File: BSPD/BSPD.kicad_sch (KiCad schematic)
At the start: 31 parts, among them Q101 Q_PMOS_GSD, U101 641964-1, U102 641964-1, U103 R-78E5.0-0.5, U104 SN74LVC1G08DBVR, U105 LM339DR, U106 NE555DR, U107 SN74LVC3G14DCUR, U108 SN74AC32DR, U109 SN74LVC1G08DBVR, U110 641964-1

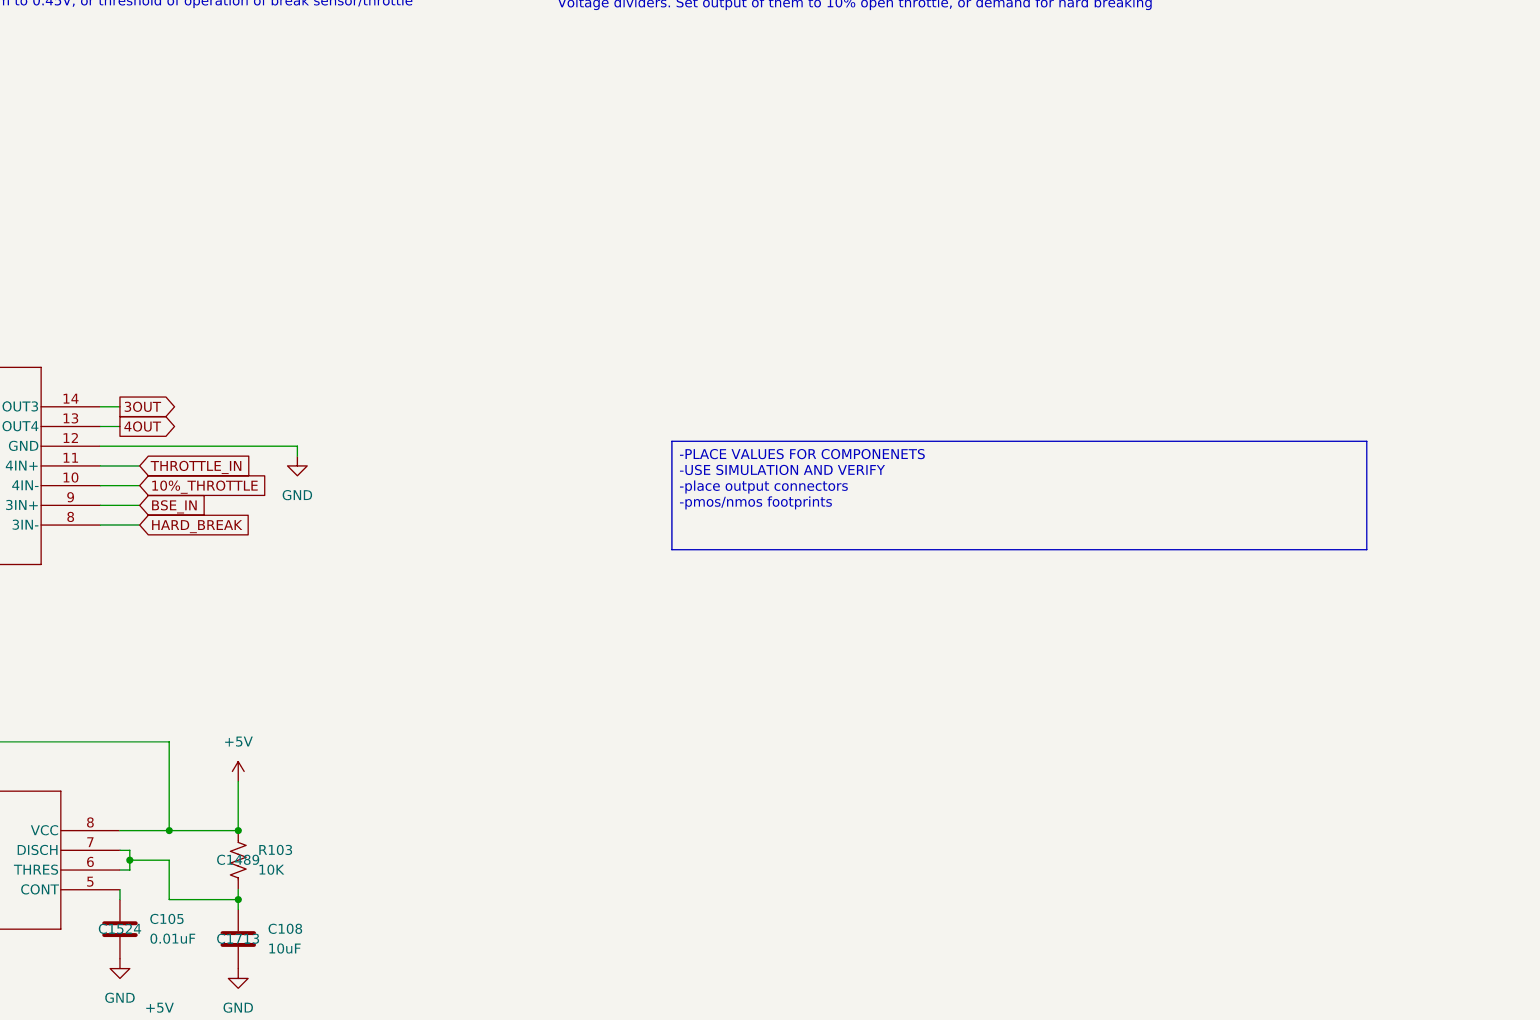
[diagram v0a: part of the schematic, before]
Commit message: Double checked PMOS output logic. Added connector and routing for sense wires from sensors. Connected one unconnected track. 2 DRC errors about spokes, but otherwise Ready to Geaux :3
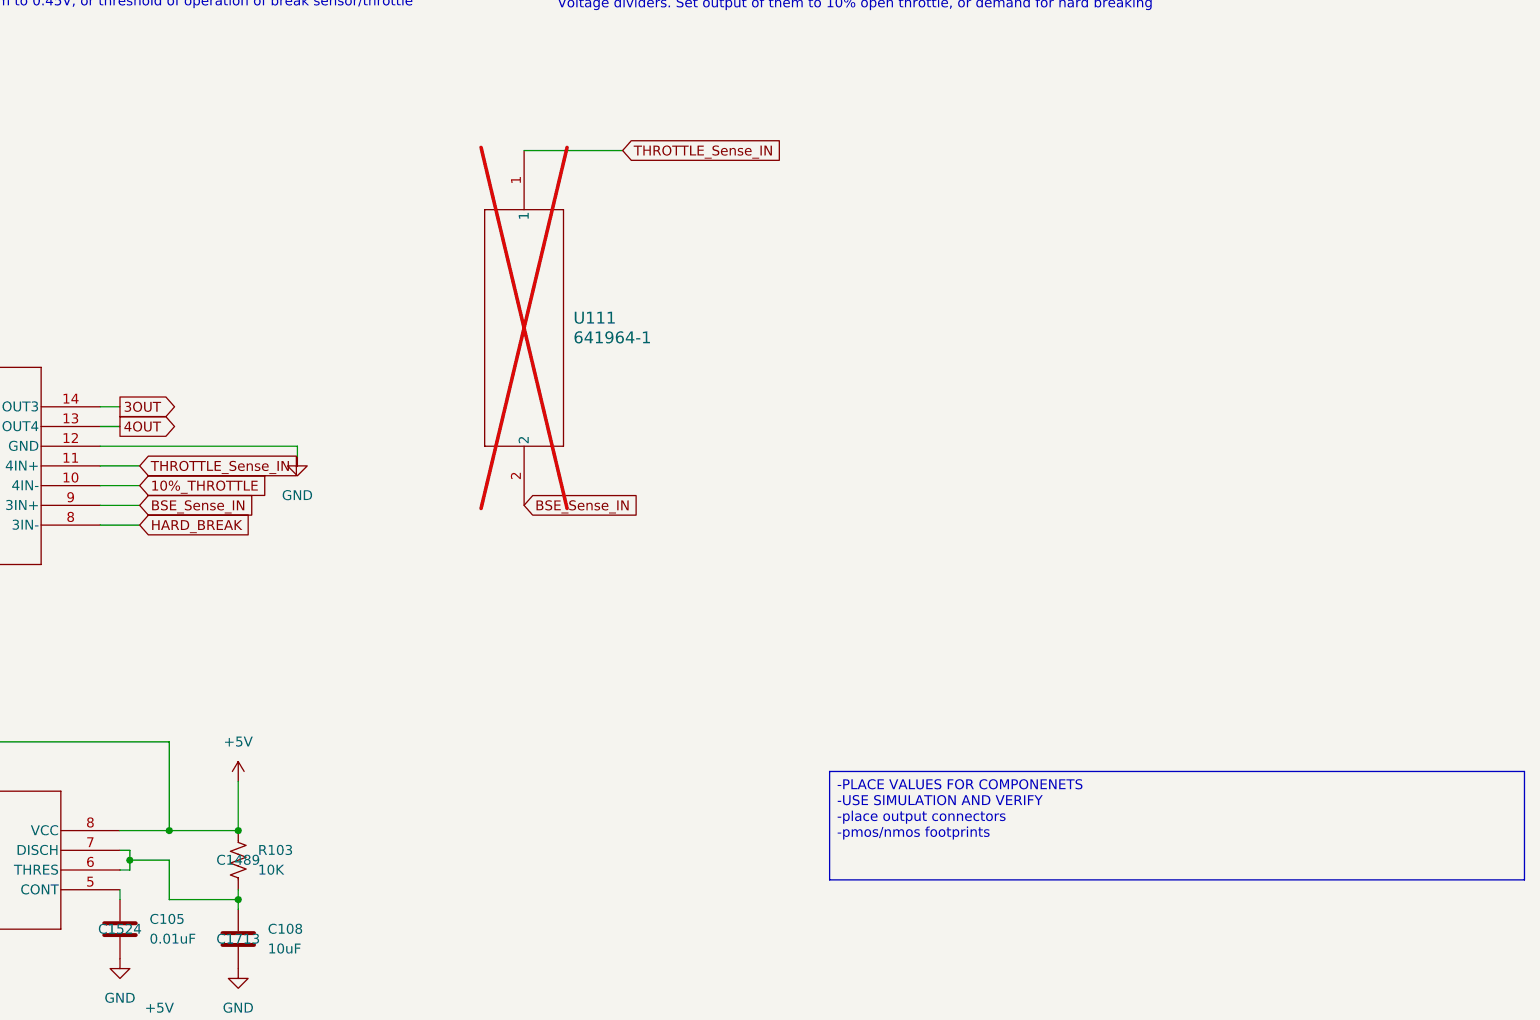
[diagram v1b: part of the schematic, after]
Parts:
- added U111: 641964-1, 641964-1:641964-1_TYC, symbol 641964-1:641964-1
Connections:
- net BSE_IN: no longer U105.9 (3IN+)
- net THROTTLE_IN: no longer U105.11 (4IN+)
- new net BSE_Sense_IN: U105.9 (3IN+), U111.2
- new net THROTTLE_Sense_IN: U105.11 (4IN+), U111.1
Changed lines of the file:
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@@
 	(text_box "-PLACE VALUES FOR COMPONENETS\n-USE SIMULATION AND VERIFY\n-place output connectors\n-pmos/nmos footprints\n\n"
 		(exclude_from_sim no)
-		(at 300.99 109.855 0)
+		(at 321.31 152.4 0)
 		(size 89.535 13.97)
 		(margins 0.9525 0.9525 0.9525 0.9525)
@@
 	(wire
 		(pts
+			(xy 294.64 72.39) (xy 281.94 72.39)
+		)
+		(stroke
+			(width 0)
+			(type default)
+		)
+	)
+	(wire
+		(pts
 			(xy 229.87 167.64) (xy 229.87 168.91)
 		)
@@
 		)
 	)
+	(global_label "BSE_Sense_IN"
+		(shape input)
+		(at 281.94 118.11 0)
+		(fields_autoplaced yes)
+		(effects
+			(font
+				(size 1.27 1.27)
+			)
+			(justify left)
+		)
+		(property "Intersheetrefs" "${INTERSHEET_REFS}"
+			(at 297.988 118.11 0)
+			(effects
+				(font
+					(size 1.27 1.27)
+				)
+				(justify left)
+				(hide yes)
+			)
+		)
+	)
 	(global_label "THRESH_BSE"
 		(shape input)
@@
 		)
 	)
-	(global_label "THROTTLE_IN"
+	(global_label "THROTTLE_Sense_IN"
 		(shape input)
 		(at 232.41 113.03 0)
@@
 		)
 		(property "Intersheetrefs" "${INTERSHEET_REFS}"
-			(at 247.309 113.03 0)
+			(at 253.8404 113.03 0)
 			(effects
 				(font
@@
 		)
 	)
-	(global_label "BSE_IN"
+	(global_label "BSE_Sense_IN"
 		(shape input)
 		(at 232.41 118.11 0)
@@
 		)
 		(property "Intersheetrefs" "${INTERSHEET_REFS}"
-			(at 241.9266 118.11 0)
+			(at 248.458 118.11 0)
 			(effects
 				(font
@@
 		)
 	)
+	(global_label "THROTTLE_Sense_IN"
+		(shape input)
+		(at 294.64 72.39 0)
+		(fields_autoplaced yes)
+		(effects
+			(font
+				(size 1.27 1.27)
+			)
+			(justify left)
+		)
+		(property "Intersheetrefs" "${INTERSHEET_REFS}"
+			(at 316.0704 72.39 0)
+			(effects
+				(font
+					(size 1.27 1.27)
+				)
+				(justify left)
+				(hide yes)
+			)
+		)
+	)
 	(global_label "THRESH_THROTTLE"
 		(shape input)
@@
 					(unit 1)
 				)
+			)
+		)
+	)
+	(symbol
+		(lib_id "641964-1:641964-1")
+		(at 281.94 72.39 270)
+		(unit 1)
+		(exclude_from_sim no)
+		(in_bom yes)
+		(on_board yes)
+		(dnp yes)
+		(fields_autoplaced yes)
+		(property "Reference" "U111"
+			(at 288.29 93.9799 90)
+			(effects
+				(font
+					(size 1.524 1.524)
+				)
+				(justify left)
+			)
+		)
+		(property "Value" "641964-1"
+			(at 288.29 96.5199 90)
+			(effects
+				(font
+					(size 1.524 1.524)
+				)
+				(justify left)
+			)
+		)
+		(property "Footprint" "641964-1:641964-1_TYC"
+			(at 281.94 72.39 0)
+			(effects
+				(font
+					(size 1.27 1.27)
+					(italic yes)
+				)
+				(hide yes)
+			)
+		)
+		(property "Datasheet" "641964-1"
+			(at 281.94 72.39 0)
+			(effects
+				(font
+					(size 1.27 1.27)
+					(italic yes)
+				)
+				(hide yes)
+			)
+		)
+		(property "Description" ""
+			(at 281.94 72.39 0)
+			(effects
+				(font
+					(size 1.27 1.27)
+				)
+				(hide yes)
+			)
+		)
+		(property "JLCPCB Part #" ""
+			(at 281.94 72.39 0)
+			(effects
+				(font
+					(size 1.27 1.27)
+				)
+			)
+		)
+		(property "Sim.Device" ""
+			(at 281.94 72.39 0)
+			(effects
+				(font
+					(size 1.27 1.27)
+				)
+			)
+		)
+		(property "Sim.Pins" ""
+			(at 281.94 72.39 0)
+			(effects
+				(font
+					(size 1.27 1.27)
+				)
+			)
+		)
+		(property "Sim.Type" ""
+			(at 281.94 72.39 0)
+			(effects
+				(font
+					(size 1.27 1.27)
+				)
+			)
+		)
+		(pin "2"
+		)
+		(pin "1"
+		)
+		(instances
+			(project "BSPD"
+				(path "/8d21c8dd-e639-4839-877d-5028bdc6290a"
+					(reference "U111")
+					(unit 1)
+				)

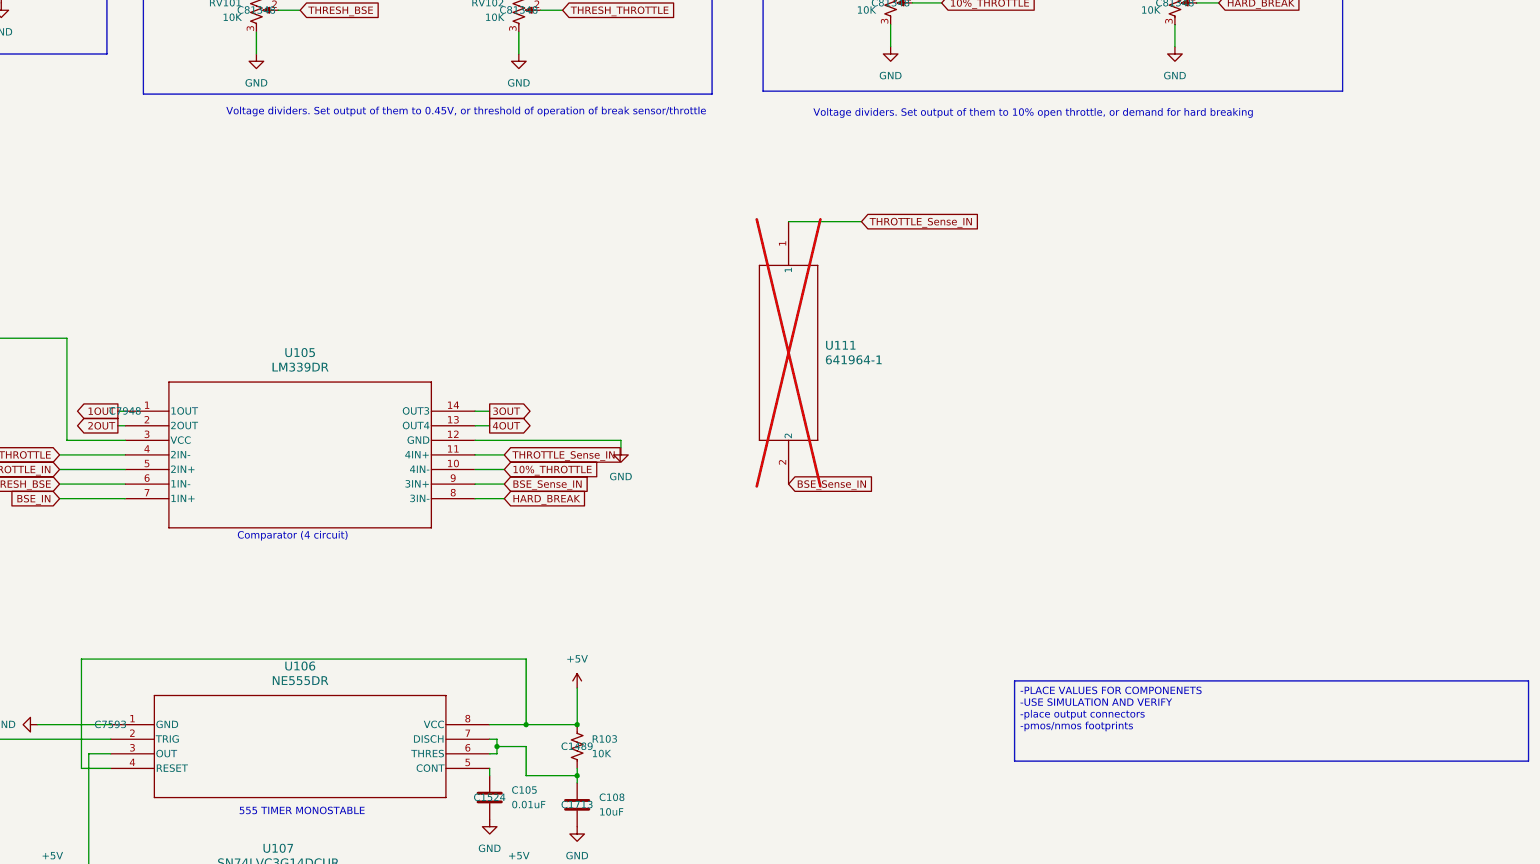
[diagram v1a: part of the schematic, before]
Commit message: Fault Latch Updated and generated gerber files
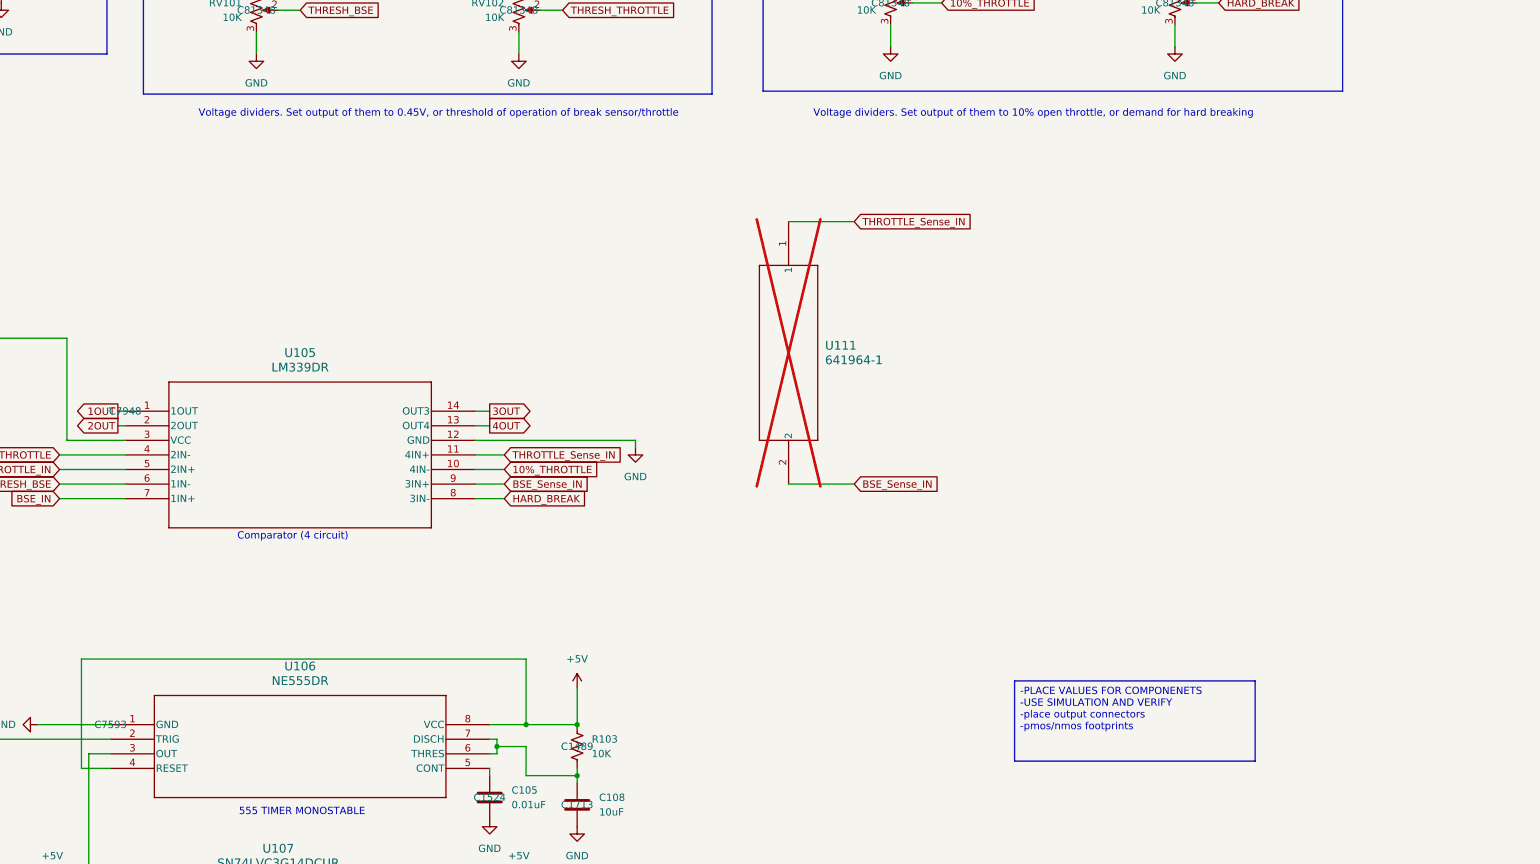
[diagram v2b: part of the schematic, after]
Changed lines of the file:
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@@
 	(text "Voltage dividers. Set output of them to 0.45V, or threshold of operation of break sensor/throttle\n"
 		(exclude_from_sim no)
-		(at 225.806 53.34 0)
+		(at 220.98 53.594 0)
 		(effects
 			(font
@@
 		(exclude_from_sim no)
 		(at 321.31 152.4 0)
-		(size 89.535 13.97)
+		(size 41.91 13.97)
 		(margins 0.9525 0.9525 0.9525 0.9525)
 		(stroke
@@
 	(wire
 		(pts
+			(xy 281.94 118.11) (xy 293.37 118.11)
+		)
+		(stroke
+			(width 0)
+			(type default)
+		)
+	)
+	(wire
+		(pts
 			(xy 323.85 207.01) (xy 309.88 207.01)
 		)
@@
 	(wire
 		(pts
-			(xy 294.64 72.39) (xy 281.94 72.39)
+			(xy 293.37 72.39) (xy 281.94 72.39)
 		)
 		(stroke
@@
 	(wire
 		(pts
-			(xy 252.73 110.49) (xy 227.33 110.49)
+			(xy 255.27 110.49) (xy 227.33 110.49)
 		)
 		(stroke
@@
 	(wire
 		(pts
-			(xy 252.73 111.76) (xy 252.73 110.49)
+			(xy 255.27 111.76) (xy 255.27 110.49)
 		)
 		(stroke
@@
 	(global_label "BSE_Sense_IN"
 		(shape input)
-		(at 281.94 118.11 0)
+		(at 293.37 118.11 0)
 		(fields_autoplaced yes)
 		(effects
@@
 		)
 		(property "Intersheetrefs" "${INTERSHEET_REFS}"
-			(at 297.988 118.11 0)
+			(at 309.418 118.11 0)
 			(effects
 				(font
@@
 	(global_label "THROTTLE_Sense_IN"
 		(shape input)
-		(at 294.64 72.39 0)
+		(at 293.37 72.39 0)
 		(fields_autoplaced yes)
 		(effects
@@
 		)
 		(property "Intersheetrefs" "${INTERSHEET_REFS}"
-			(at 316.0704 72.39 0)
+			(at 314.8004 72.39 0)
 			(effects
 				(font
@@
 	(symbol
 		(lib_id "power:GND")
-		(at 252.73 111.76 0)
+		(at 255.27 111.76 0)
 		(unit 1)
 		(exclude_from_sim no)
@@
 		(fields_autoplaced yes)
 		(property "Reference" "#PWR0121"
-			(at 252.73 118.11 0)
+			(at 255.27 118.11 0)
 			(effects
 				(font
@@
 		)
 		(property "Value" "GND"
-			(at 252.73 116.84 0)
+			(at 255.27 116.84 0)
 			(effects
 				(font
@@
 		)
 		(property "Footprint" ""
-			(at 252.73 111.76 0)
+			(at 255.27 111.76 0)
 			(effects
 				(font
@@
 		)
 		(property "Datasheet" ""
-			(at 252.73 111.76 0)
+			(at 255.27 111.76 0)
 			(effects
 				(font
@@
 		)
 		(property "Description" "Power symbol creates a global label with name \"GND\" , ground"
-			(at 252.73 111.76 0)
-			(effects
-				(font
+			(at 255.27 111.76 0)
+			(effects
+				(font
